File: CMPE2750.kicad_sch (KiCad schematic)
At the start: 2 parts, among them U1 STM32L476VGTx

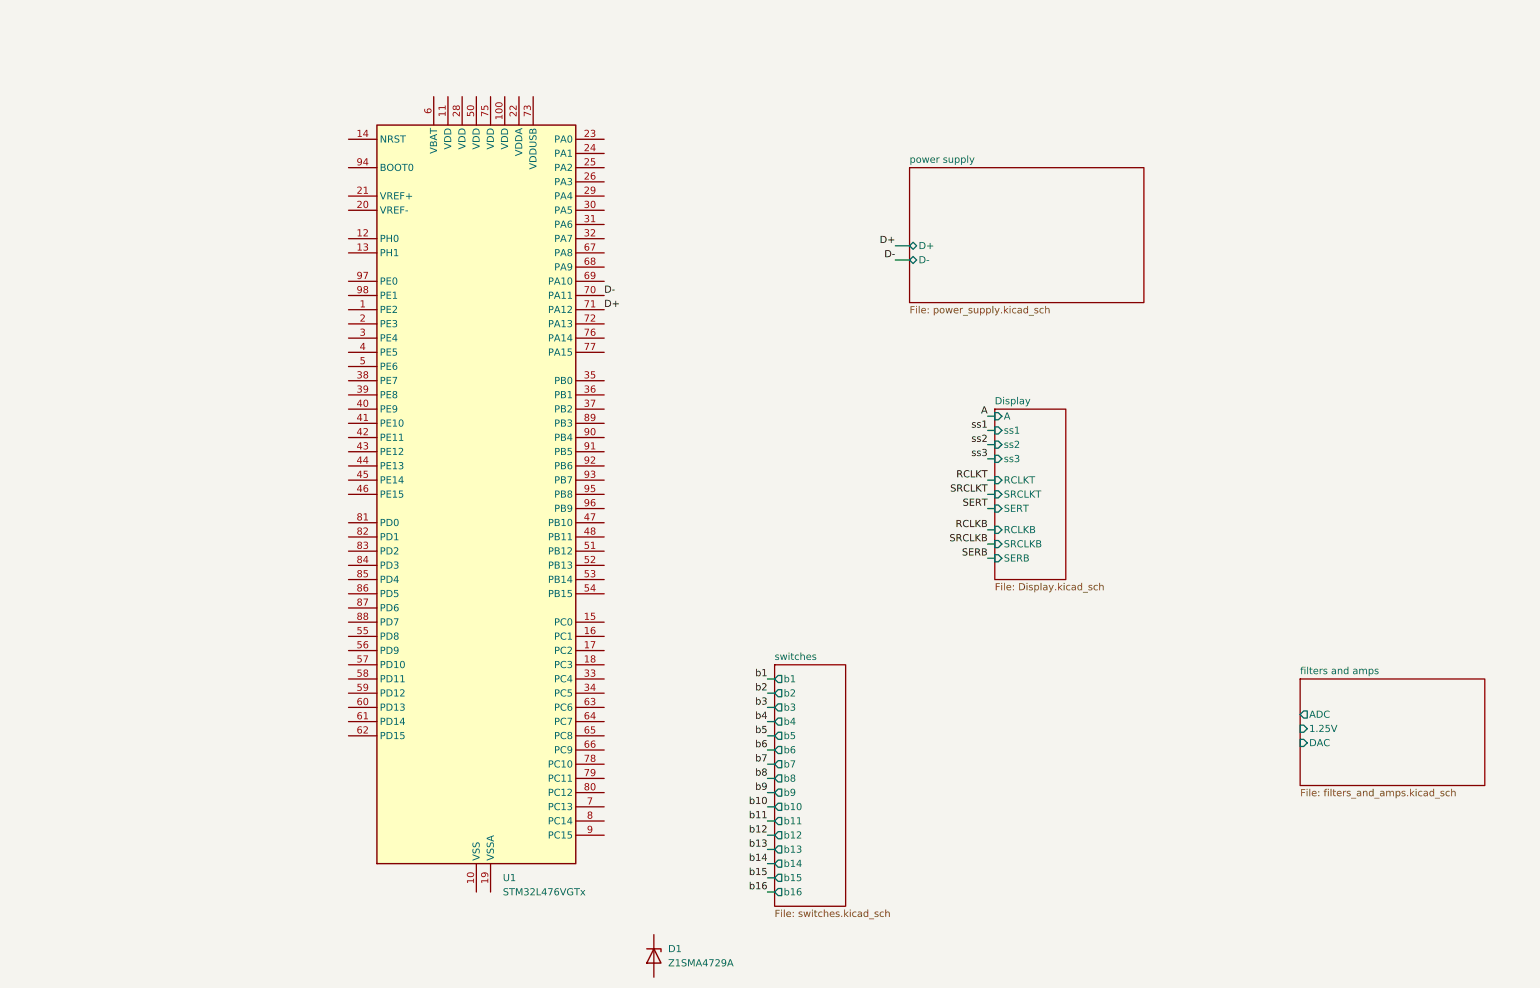
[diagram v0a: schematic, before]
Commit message: Changed how the 14-segment displays were controlled to just use a couple shift registers
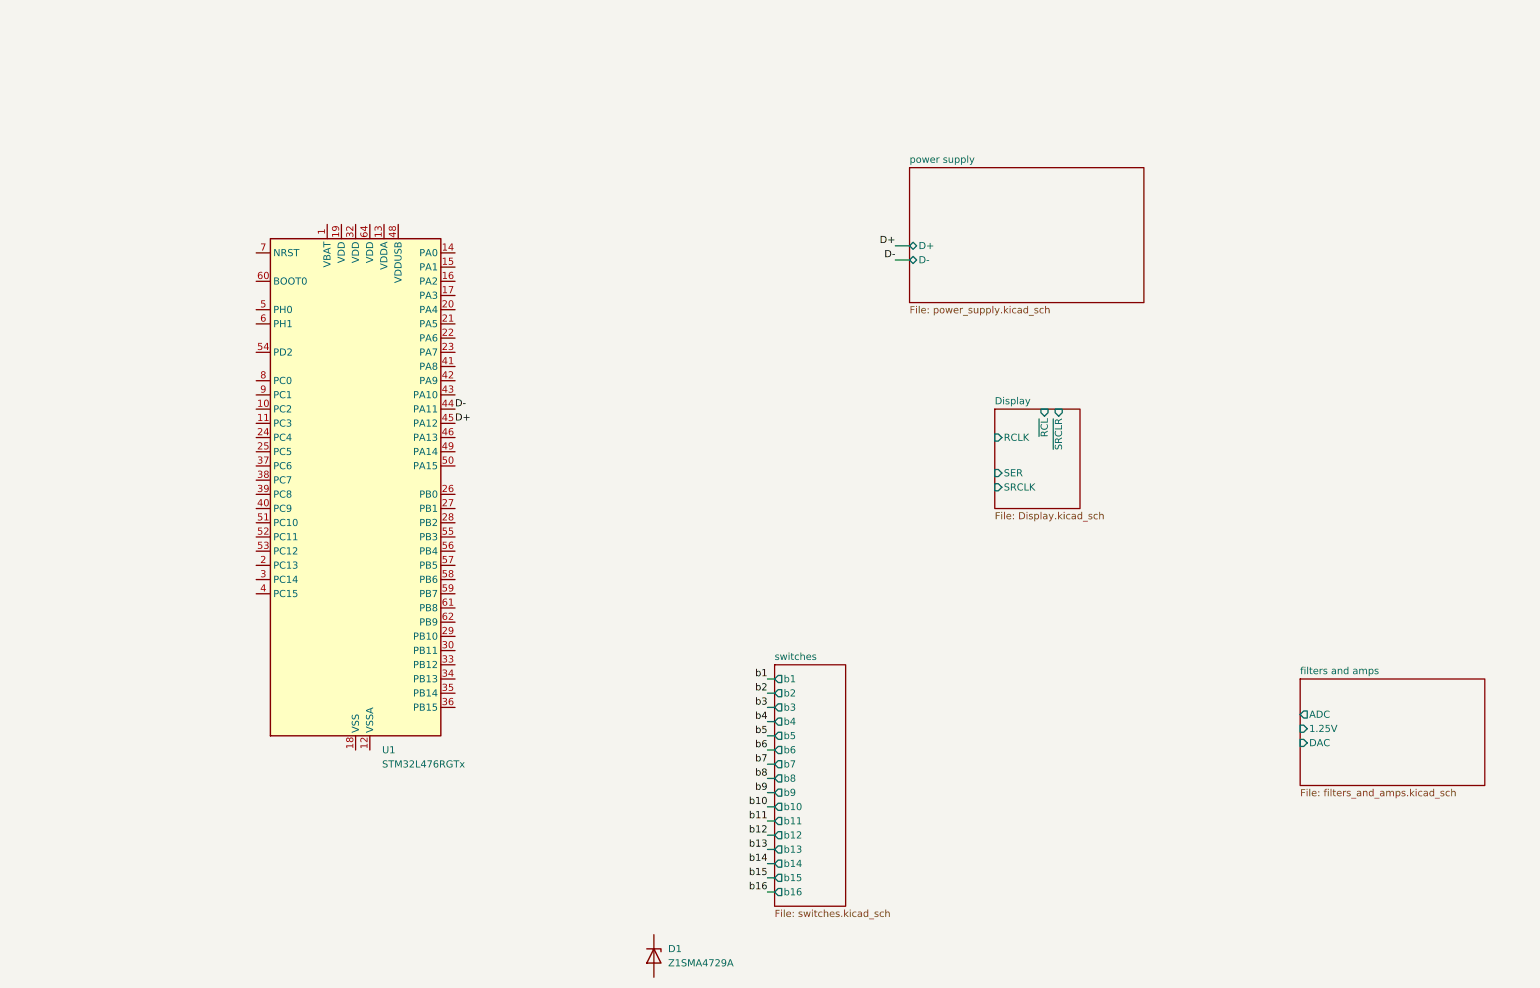
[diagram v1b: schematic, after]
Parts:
- removed U1: STM32L476VGTx, Package_QFP:LQFP-100_14x14mm_P0.5mm, symbol MCU_ST_STM32L4:STM32L476VGTx
- added U1: STM32L476RGTx, Package_QFP:LQFP-64_10x10mm_P0.5mm, symbol MCU_ST_STM32L4:STM32L476RGTx
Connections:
- net D+: now also U1.45 (PA12)
- net D-: now also U1.44 (PA11)
- new net: U1.18 (VSS), U1.31 (VSS), U1.47 (VSS), U1.63 (VSS)
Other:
- sheet Display ports: added RCLK, SER, SRCLK, ~{RCL}, ~{SRCLR}; removed A, RCLKB, RCLKT, SERB, SERT, SRCLKB, SRCLKT, ss1, ss2, ss3

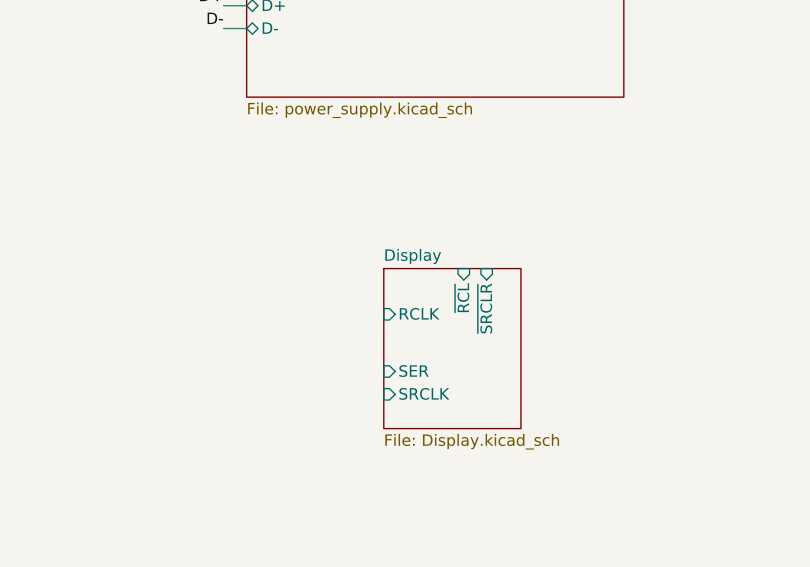
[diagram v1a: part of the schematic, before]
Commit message: Finished the display and input switch schematics. Also added input buffers to the inputs and made them differential
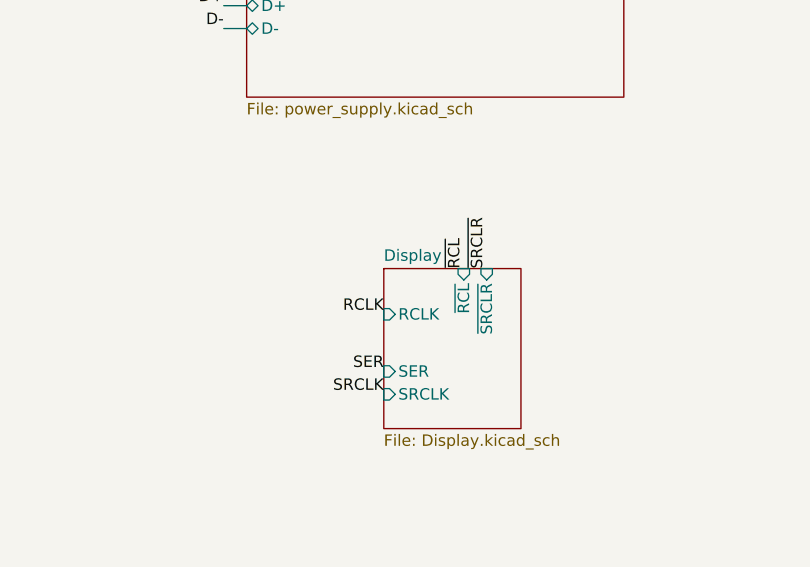
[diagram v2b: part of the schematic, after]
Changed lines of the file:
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@@
+		)
+	)
+	(label "RCLK"
+		(at 190.5 93.98 180)
+		(effects
+			(font
+				(size 1.27 1.27)
+			)
+			(justify right bottom)
 		)
 	)
@@
 		)
 	)
+	(label "SER"
+		(at 190.5 100.33 180)
+		(effects
+			(font
+				(size 1.27 1.27)
+			)
+			(justify right bottom)
+		)
+	)
 	(label "b1"
 		(at 149.86 137.16 180)
@@
 		)
 	)
+	(label "~{RCL}"
+		(at 199.39 88.9 90)
+		(effects
+			(font
+				(size 1.27 1.27)
+			)
+			(justify left bottom)
+		)
+	)
+	(label "SRCLK"
+		(at 190.5 102.87 180)
+		(effects
+			(font
+				(size 1.27 1.27)
+			)
+			(justify right bottom)
+		)
+	)
 	(label "b6"
 		(at 149.86 149.86 180)
@@
 		)
 	)
+	(label "~{SRCLR}"
+		(at 201.93 88.9 90)
+		(effects
+			(font
+				(size 1.27 1.27)
+			)
+			(justify left bottom)
+		)
+	)

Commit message: Almost done. Just going to try and change something
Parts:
- removed D1: Z1SMA4729A, Diode_SMD:D_SMA, symbol Diode:Z1SMAxxx
- added C22, C23, C24, C25, C26, C27, C28: 100nF, LMK212G_TAY, symbol CMPE2750:LMK212B7105KGHTR
- added FB1: FerriteBead, symbol Device:FerriteBead_Small
- added J10: Conn_01x16, symbol Connector_Generic:Conn_01x16
- added J5: Conn_02x07_Odd_Even, symbol Connector_Generic:Conn_02x07_Odd_Even
- added J6: SPI3, symbol Connector_Generic:Conn_02x04_Counter_Clockwise
- added J7: Conn_02x16_Top_Bottom, symbol Connector_Generic:Conn_02x16_Top_Bottom
- added J8: Conn_01x04, symbol Connector_Generic:Conn_01x04
- added R133, R134, R135, R136: 10kΩ, symbol Device:R_US
- added SW3: D6R90F1LFS, D6R_CNK, symbol CMPE2750:D6R90F1LFS
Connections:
- net b1: now also U1.26 (PB0), J10.1 (Pin_1)
- net b10: now also U1.62 (PB9), J10.10 (Pin_10)
- net b11: now also U1.29 (PB10), J10.11 (Pin_11)
- net b12: now also U1.30 (PB11), J10.12 (Pin_12)
- net b13: now also U1.33 (PB12), J10.13 (Pin_13)
- net b14: now also U1.34 (PB13), J10.14 (Pin_14)
- net b15: now also U1.35 (PB14), J10.15 (Pin_15)
- net b16: now also U1.36 (PB15), J10.16 (Pin_16)
- net b2: now also U1.27 (PB1), J10.2 (Pin_2)
- net b3: now also U1.28 (PB2), J10.3 (Pin_3)
- net b4: now also U1.55 (PB3), J10.4 (Pin_4)
- net b5: now also U1.56 (PB4), J10.5 (Pin_5)
- net b6: now also U1.57 (PB5), J10.6 (Pin_6)
- net b7: now also U1.58 (PB6), J10.7 (Pin_7)
- net b8: now also U1.59 (PB7), J10.8 (Pin_8)
- net b9: now also U1.61 (PB8), J10.9 (Pin_9)
- net ~{RCL}: now also U1.25 (PC5), J7.6 (Pin_6), R134.1
- net ~{SRCLR}: now also U1.24 (PC4), J7.5 (Pin_5), R135.1
- net VDD: now reaches U1.1 (VBAT)
- net VDD: now also U1.19 (VDD), U1.32 (VDD), U1.48 (VDDUSB), U1.64 (VDD), C22.1, C23.1, C24.1, C25.1, C26.1, FB1.1, J5.3 (Pin_3), J7.18 (Pin_18)
- net PC2: now reaches U1.10 (PC2)
- net PC2: now also J7.3 (Pin_3)
- net PC3: now reaches U1.11 (PC3)
- net PC3: now also J7.4 (Pin_4)
- net GND: now reaches U1.12 (VSSA)
- net GND: now also U1.18 (VSS), U1.31 (VSS), U1.47 (VSS), U1.63 (VSS), C22.2, C23.2, C24.2, C25.2, C26.2, C27.2, J5.11 (Pin_11), J5.5 (Pin_5), J5.7 (Pin_7), J7.19 (Pin_19), J8.4 (Pin_4), R133.2, R134.2, R135.2, R136.1, SW3.2
- net VDDA: now reaches U1.13 (VDDA)
- net VDDA: now also C27.1, FB1.2, J7.16 (Pin_16)
- net PA0: now reaches U1.14 (PA0)
- net PA0: now also J7.21 (Pin_21)
- net PA1: now reaches U1.15 (PA1)
- net PA1: now also J7.22 (Pin_22)
- net PA2: now reaches U1.16 (PA2)
- net PA2: now also J7.23 (Pin_23)
- net PA3: now reaches U1.17 (PA3)
- net PA3: now also J7.24 (Pin_24)
- net PC13: now reaches U1.2 (PC13)
- net PC13: now also J7.11 (Pin_11)
- net DAC: now reaches U1.20 (PA4)
- net DAC: now also J7.25 (Pin_25)
- net 1.25V: now reaches U1.21 (PA5)
- net 1.25V: now also J7.26 (Pin_26)
- net PA6: now reaches U1.22 (PA6)
- net PA6: now also J7.27 (Pin_27)
- net PA7: now reaches U1.23 (PA7)
- net PA7: now also J7.28 (Pin_28)
- net PC14: now reaches U1.3 (PC14)
- net PC14: now also J7.12 (Pin_12)
- net PC6: now reaches U1.37 (PC6)
- net PC6: now also J7.7 (Pin_7)
- net PC7: now reaches U1.38 (PC7)
- net PC7: now also J7.8 (Pin_8)
- net PC8: now reaches U1.39 (PC8)
- net PC8: now also J7.9 (Pin_9)
- net PC15: now reaches U1.4 (PC15)
- net PC15: now also J7.13 (Pin_13)
- net PC9: now reaches U1.40 (PC9)
- net PC9: now also J7.10 (Pin_10)
- net PA8: now reaches U1.41 (PA8)
- net PA8: now also J7.29 (Pin_29)
- net at U1.42 (PA9): now also J5.14 (Pin_14)
- net at U1.43 (PA10): now also J5.13 (Pin_13)
- net at U1.46 (PA13): now also J5.4 (Pin_4)
- net at U1.49 (PA14): now also J5.6 (Pin_6)
- net PH0: now reaches U1.5 (PH0)
- net PH0: now also J7.30 (Pin_30)
- net RCLK/CS: now reaches U1.50 (PA15)
- net RCLK/CS: now also J6.4 (Pin_4)
- net SRCLK/CLK: now reaches U1.51 (PC10)
- net SRCLK/CLK: now also J6.3 (Pin_3)
- net SO/MISO: now reaches U1.52 (PC11)
- net SO/MISO: now also J6.2 (Pin_2)
- net SER/MOSI: now reaches U1.53 (PC12)
- net SER/MOSI: now also J6.1 (Pin_1)
- net PD2: now reaches U1.54 (PD2)
- net PD2: now also J7.32 (Pin_32)
- net PH1: now reaches U1.6 (PH1)
- net PH1: now also J7.31 (Pin_31)
- net BOOT0: now reaches U1.60 (BOOT0)
- net BOOT0: now also J7.15 (Pin_15), R133.1
- net NRST: now reaches U1.7 (NRST)
- net NRST: now also J5.12 (Pin_12), J7.14 (Pin_14), SW3.1
- net ADC: now reaches U1.8 (PC0)
- net ADC: now also J7.1 (Pin_1)
- net PC1: now reaches U1.9 (PC1)
- net PC1: now also J7.2 (Pin_2)
- new net: C28.2, SW3.3
- new net: C28.1, SW3.4
- new net -5V: J7.20 (Pin_20)
- new net Display/RCLK: J6.5 (Pin_5)
- new net Display/SER: J6.8 (Pin_8)
- new net Display/SO: J6.7 (Pin_7), R136.2
- new net Display/SRCLK: J6.6 (Pin_6)
- new net MAIN_INPUT+: J8.2 (Pin_2)
- new net MAIN_INPUT-: J8.3 (Pin_3)
- new net OUT+: J8.1 (Pin_1)
- new net VBUS: J7.17 (Pin_17)
- no-connect marks 0 -> 5
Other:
- sheet Display ports: added SO; removed none

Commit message: Schematic is done?
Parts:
- added C29, C30: 3.8 pF, Capacitor_SMD:C_0402_1005Metric, symbol Device:C
- added R137, R138: 10kΩ, Resistor_SMD:R_0402_1005Metric, symbol CMPE2750:0402WGJ0103TCE
- added X1: ABS25-32.768KHZ-6-T, X_ABS25_ABR, symbol CMPE2750:ABS25-32.768KHZ-6-T
- C22, C23, C24, C25, C26, C27, C28: footprint LMK212G_TAY -> Capacitor_SMD:C_0402_1005Metric; symbol CMPE2750:LMK212B7105KGHTR -> CMPE2750:CL05B104KP5NNNC
- FB1: footprint (none) -> Inductor_SMD:L_0603_1608Metric
- J10: footprint (none) -> Connector_PinHeader_2.54mm:PinHeader_1x06_P2.54mm_Vertical
- J5: footprint (none) -> Connector_PinHeader_1.27mm:PinHeader_2x07_P1.27mm_Vertical
- J6: footprint (none) -> Connector_PinHeader_2.54mm:PinHeader_2x04_P2.54mm_Vertical
- J7: footprint (none) -> Connector_PinHeader_2.54mm:PinHeader_2x06_P2.54mm_Vertical
- J8: footprint (none) -> Connector_PinHeader_2.54mm:PinHeader_1x04_P2.54mm_Vertical
- R133, R134, R135, R136: footprint (none) -> Resistor_SMD:R_0402_1005Metric; symbol Device:R_US -> CMPE2750:0402WGJ0103TCE
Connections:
- net BOOT0: now also J7.13 (Pin_13); no longer J7.15 (Pin_15)
- net GND: now also C29.2, C30.2
- net MAIN_INPUT+: now also R138.1; no longer J8.2 (Pin_2)
- net MAIN_INPUT-: now also R137.1; no longer J8.3 (Pin_3)
- net NRST: now also J7.12 (Pin_12); no longer J7.14 (Pin_14)
- net PC14 renamed RCC_OSC32_IN
- net RCC_OSC32_IN: now also C29.1, X1.1 (CRYSTAL); no longer J7.12 (Pin_12)
- net PC15 renamed RCC_OSC32_OUT
- net RCC_OSC32_OUT: now also C30.1, X1.4 (CRYSTAL); no longer J7.13 (Pin_13)
- new net: J8.3 (Pin_3), R137.2
- new net: J8.2 (Pin_2), R138.2
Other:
- note added: "To be placed as close as possible to RCC_OSC32_IN/OUT"

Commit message: *Now* it's finished. Maybe.
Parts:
- added R139, R140, R141, R142, R143, R144, R145, R146, R147, R148, R149, R150, R151, R152, R153, R154, R155, R156: 10kΩ, Resistor_SMD:R_0402_1005Metric, symbol CMPE2750:0402WGJ0103TCE
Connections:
- net GND: now also R139.2, R140.2, R141.2, R142.2, R143.2, R144.2, R145.2, R146.2, R147.2, R148.2, R149.2, R150.2, R151.2, R152.2, R153.2, R154.2, R155.2, R156.2
- net PA0: now also R139.1
- net PA1: now also R140.1
- net PA2: now also R141.1
- net PA3: now also R142.1
- net PA6: now also R143.1
- net PA7: now also R144.1
- net PA8: now also R145.1
- net PC1: now also R149.1
- net PC13: now also R156.1
- net PC2: now also R150.1
- net PC3: now also R151.1
- net PC6: now also R152.1
- net PC7: now also R153.1
- net PC8: now also R154.1
- net PC9: now also R155.1
- net PD2: now also R148.1
- net PH0: now also R146.1
- net PH1: now also R147.1

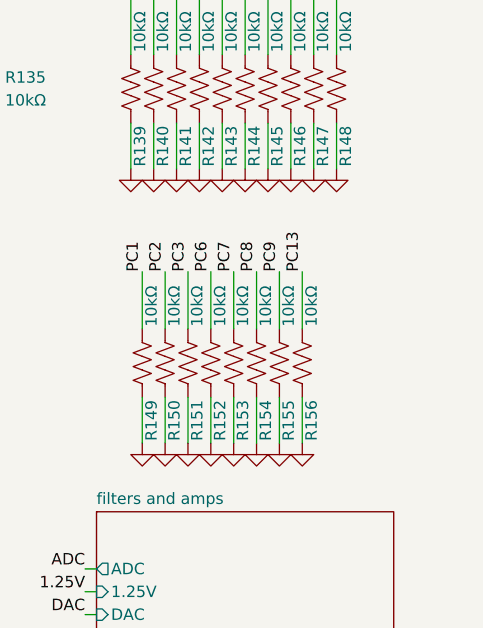
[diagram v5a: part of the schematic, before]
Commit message: Swapped the current limiting diodes for resistors. They *should* be good enough under normal operating conditions. Also added some pull-down resistors. Done?
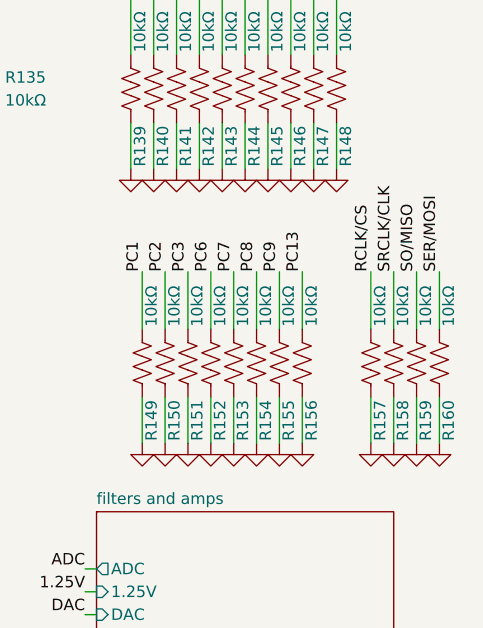
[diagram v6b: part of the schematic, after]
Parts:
- added R157, R158, R159, R160: 10kΩ, Resistor_SMD:R_0402_1005Metric, symbol CMPE2750:0402WGJ0103TCE
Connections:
- net GND: now also R157.2, R158.2, R159.2, R160.2
- net RCLK/CS: now also R157.1
- net SER/MOSI: now also R160.1
- net SO/MISO: now also R159.1
- net SRCLK/CLK: now also R158.1
